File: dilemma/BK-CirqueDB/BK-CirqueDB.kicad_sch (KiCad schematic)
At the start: 9 parts, among them J1 CirqueDB

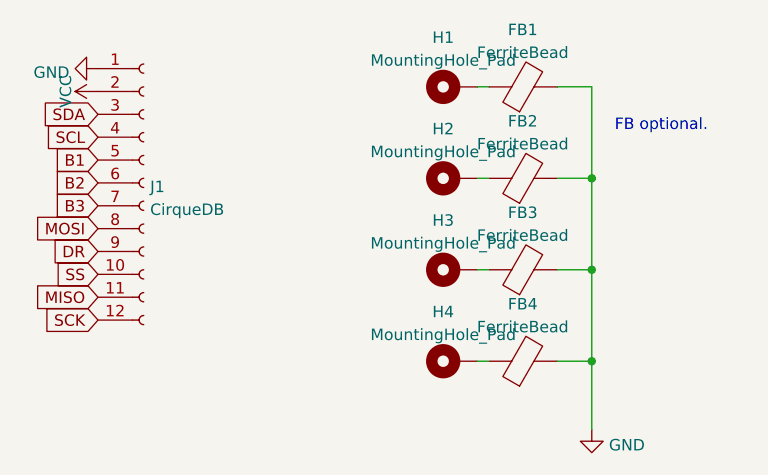
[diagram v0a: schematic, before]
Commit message: make trackpad pinout compatible with oled
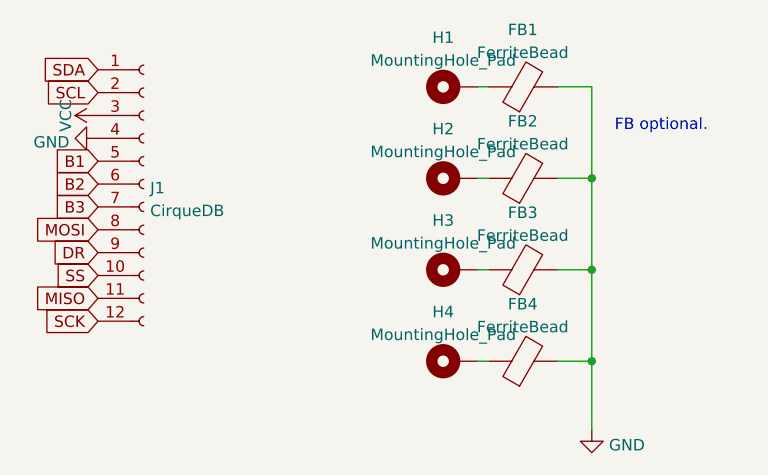
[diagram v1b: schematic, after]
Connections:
- net GND: now also J1.4 (Pin_4); no longer J1.1 (Pin_1)
- net SCL: now also J1.2 (Pin_2); no longer J1.4 (Pin_4)
- net SDA: now also J1.1 (Pin_1); no longer J1.3 (Pin_3)
- net VCC: now also J1.3 (Pin_3); no longer J1.2 (Pin_2)
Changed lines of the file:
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@@
     (effects (font (size 1.27 1.27)) (justify left bottom))
   )
-  (global_label "B1" (shape input) (at 27.94 33.528 180) (fields_autoplaced)
-    (effects (font (size 1.27 1.27)) (justify right))
-    (property "Intersheet References" "${INTERSHEET_REFS}" (id 0) (at 23.0474 33.4486 0)
-      (effects (font (size 1.27 1.27)) (justify right) hide)
-    )
-  )
-  (global_label "MOSI" (shape input) (at 27.94 41.148 180) (fields_autoplaced)
-    (effects (font (size 1.27 1.27)) (justify right))
-    (property "Intersheet References" "${INTERSHEET_REFS}" (id 0) (at 20.9307 41.0686 0)
-      (effects (font (size 1.27 1.27)) (justify right) hide)
-    )
-  )
-  (global_label "DR" (shape input) (at 27.94 43.688 180) (fields_autoplaced)
-    (effects (font (size 1.27 1.27)) (justify right))
-    (property "Intersheet References" "${INTERSHEET_REFS}" (id 0) (at 22.9869 43.6086 0)
-      (effects (font (size 1.27 1.27)) (justify right) hide)
-    )
-  )
-  (global_label "B3" (shape input) (at 27.94 38.608 180) (fields_autoplaced)
-    (effects (font (size 1.27 1.27)) (justify right))
-    (property "Intersheet References" "${INTERSHEET_REFS}" (id 0) (at 23.0474 38.5286 0)
-      (effects (font (size 1.27 1.27)) (justify right) hide)
-    )
-  )
-  (global_label "MISO" (shape input) (at 27.94 48.768 180) (fields_autoplaced)
-    (effects (font (size 1.27 1.27)) (justify right))
-    (property "Intersheet References" "${INTERSHEET_REFS}" (id 0) (at 20.9307 48.6886 0)
-      (effects (font (size 1.27 1.27)) (justify right) hide)
-    )
-  )
-  (global_label "B2" (shape input) (at 27.94 36.068 180) (fields_autoplaced)
-    (effects (font (size 1.27 1.27)) (justify right))
-    (property "Intersheet References" "${INTERSHEET_REFS}" (id 0) (at 23.0474 35.9886 0)
-      (effects (font (size 1.27 1.27)) (justify right) hide)
-    )
-  )
-  (global_label "SDA" (shape input) (at 27.94 28.448 180) (fields_autoplaced)
-    (effects (font (size 1.27 1.27)) (justify right))
-    (property "Intersheet References" "${INTERSHEET_REFS}" (id 0) (at 21.9588 28.3686 0)
-      (effects (font (size 1.27 1.27)) (justify right) hide)
-    )
-  )
-  (global_label "SCL" (shape input) (at 27.94 30.988 180) (fields_autoplaced)
-    (effects (font (size 1.27 1.27)) (justify right))
-    (property "Intersheet References" "${INTERSHEET_REFS}" (id 0) (at 22.0193 30.9086 0)
-      (effects (font (size 1.27 1.27)) (justify right) hide)
-    )
-  )
-  (global_label "SS" (shape input) (at 27.94 46.228 180) (fields_autoplaced)
-    (effects (font (size 1.27 1.27)) (justify right))
-    (property "Intersheet References" "${INTERSHEET_REFS}" (id 0) (at 23.1079 46.1486 0)
-      (effects (font (size 1.27 1.27)) (justify right) hide)
-    )
-  )
-  (global_label "SCK" (shape input) (at 27.94 51.308 180) (fields_autoplaced)
-    (effects (font (size 1.27 1.27)) (justify right))
-    (property "Intersheet References" "${INTERSHEET_REFS}" (id 0) (at 21.7774 51.2286 0)
-      (effects (font (size 1.27 1.27)) (justify right) hide)
-    )
-  )
-  (symbol (lib_id "Connector:Conn_01x12_Female") (at 33.02 36.068 0) (unit 1)
-    (in_bom yes) (on_board yes) (fields_autoplaced)
-    (property "Reference" "J1" (id 0) (at 33.7312 36.5033 0)
+  (global_label "B1" (shape input) (at 27.94 33.655 180) (fields_autoplaced)
+    (effects (font (size 1.27 1.27)) (justify right))
+    (property "Intersheet References" "${INTERSHEET_REFS}" (id 0) (at 23.0474 33.5756 0)
+      (effects (font (size 1.27 1.27)) (justify right) hide)
+    )
+  )
+  (global_label "MOSI" (shape input) (at 27.94 41.275 180) (fields_autoplaced)
+    (effects (font (size 1.27 1.27)) (justify right))
+    (property "Intersheet References" "${INTERSHEET_REFS}" (id 0) (at 20.9307 41.1956 0)
+      (effects (font (size 1.27 1.27)) (justify right) hide)
+    )
+  )
+  (global_label "DR" (shape input) (at 27.94 43.815 180) (fields_autoplaced)
+    (effects (font (size 1.27 1.27)) (justify right))
+    (property "Intersheet References" "${INTERSHEET_REFS}" (id 0) (at 22.9869 43.7356 0)
+      (effects (font (size 1.27 1.27)) (justify right) hide)
+    )
+  )
+  (global_label "B3" (shape input) (at 27.94 38.735 180) (fields_autoplaced)
+    (effects (font (size 1.27 1.27)) (justify right))
+    (property "Intersheet References" "${INTERSHEET_REFS}" (id 0) (at 23.0474 38.6556 0)
+      (effects (font (size 1.27 1.27)) (justify right) hide)
+    )
+  )
+  (global_label "MISO" (shape input) (at 27.94 48.895 180) (fields_autoplaced)
+    (effects (font (size 1.27 1.27)) (justify right))
+    (property "Intersheet References" "${INTERSHEET_REFS}" (id 0) (at 20.9307 48.8156 0)
+      (effects (font (size 1.27 1.27)) (justify right) hide)
+    )
+  )
+  (global_label "B2" (shape input) (at 27.94 36.195 180) (fields_autoplaced)
+    (effects (font (size 1.27 1.27)) (justify right))
+    (property "Intersheet References" "${INTERSHEET_REFS}" (id 0) (at 23.0474 36.1156 0)
+      (effects (font (size 1.27 1.27)) (justify right) hide)
+    )
+  )
+  (global_label "SDA" (shape input) (at 27.94 23.495 180) (fields_autoplaced)
+    (effects (font (size 1.27 1.27)) (justify right))
+    (property "Intersheet References" "${INTERSHEET_REFS}" (id 0) (at 21.9588 23.4156 0)
+      (effects (font (size 1.27 1.27)) (justify right) hide)
+    )
+  )
+  (global_label "SCL" (shape input) (at 27.94 26.035 180) (fields_autoplaced)
+    (effects (font (size 1.27 1.27)) (justify right))
+    (property "Intersheet References" "${INTERSHEET_REFS}" (id 0) (at 22.0193 25.9556 0)
+      (effects (font (size 1.27 1.27)) (justify right) hide)
+    )
+  )
+  (global_label "SS" (shape input) (at 27.94 46.355 180) (fields_autoplaced)
+    (effects (font (size 1.27 1.27)) (justify right))
+    (property "Intersheet References" "${INTERSHEET_REFS}" (id 0) (at 23.1079 46.2756 0)
+      (effects (font (size 1.27 1.27)) (justify right) hide)
+    )
+  )
+  (global_label "SCK" (shape input) (at 27.94 51.435 180) (fields_autoplaced)
+    (effects (font (size 1.27 1.27)) (justify right))
+    (property "Intersheet References" "${INTERSHEET_REFS}" (id 0) (at 21.7774 51.3556 0)
+      (effects (font (size 1.27 1.27)) (justify right) hide)
+    )
+  )
+  (symbol (lib_id "Connector:Conn_01x12_Female") (at 33.02 36.195 0) (unit 1)
+    (in_bom yes) (on_board yes) (fields_autoplaced)
+    (property "Reference" "J1" (id 0) (at 33.7312 36.6303 0)
       (effects (font (size 1.27 1.27)) (justify left))
     )
-    (property "Value" "CirqueDB" (id 1) (at 33.7312 39.0402 0)
+    (property "Value" "CirqueDB" (id 1) (at 33.7312 39.1672 0)
       (effects (font (size 1.27 1.27)) (justify left))
     )
-    (property "Footprint" "prettylib:CirqueDB-BK" (id 2) (at 33.02 36.068 0)
-      (effects (font (size 1.27 1.27)) hide)
-    )
-    (property "Datasheet" "~" (id 3) (at 33.02 36.068 0)
+    (property "Footprint" "prettylib:CirqueDB-BK" (id 2) (at 33.02 36.195 0)
+      (effects (font (size 1.27 1.27)) hide)
+    )
+    (property "Datasheet" "~" (id 3) (at 33.02 36.195 0)
       (effects (font (size 1.27 1.27)) hide)
     )
@@
     (pin "1")
   )
-  (symbol (lib_id "power:GND") (at 27.94 23.368 270) (unit 1)
-    (in_bom yes) (on_board yes) (fields_autoplaced)
-    (property "Reference" "#PWR0104" (id 0) (at 21.59 23.368 0)
-      (effects (font (size 1.27 1.27)) hide)
-    )
-    (property "Value" "GND" (id 1) (at 24.7651 23.8018 90)
+  (symbol (lib_id "power:GND") (at 27.94 31.115 270) (unit 1)
+    (in_bom yes) (on_board yes) (fields_autoplaced)
+    (property "Reference" "#PWR0104" (id 0) (at 21.59 31.115 0)
+      (effects (font (size 1.27 1.27)) hide)
+    )
+    (property "Value" "GND" (id 1) (at 24.7651 31.5488 90)
       (effects (font (size 1.27 1.27)) (justify right))
     )
-    (property "Footprint" "" (id 2) (at 27.94 23.368 0)
-      (effects (font (size 1.27 1.27)) hide)
-    )
-    (property "Datasheet" "" (id 3) (at 27.94 23.368 0)
+    (property "Footprint" "" (id 2) (at 27.94 31.115 0)
+      (effects (font (size 1.27 1.27)) hide)
+    )
+    (property "Datasheet" "" (id 3) (at 27.94 31.115 0)
       (effects (font (size 1.27 1.27)) hide)
     )
@@
     (pin "1")
   )
-  (symbol (lib_id "power:VCC") (at 27.94 25.908 90) (unit 1)
+  (symbol (lib_id "power:VCC") (at 27.94 28.575 90) (unit 1)
     (in_bom yes) (on_board yes)
-    (property "Reference" "#PWR0103" (id 0) (at 31.75 25.908 0)
-      (effects (font (size 1.27 1.27)) hide)
-    )
-    (property "Value" "VCC" (id 1) (at 24.3642 25.908 0))
-    (property "Footprint" "" (id 2) (at 27.94 25.908 0)
-      (effects (font (size 1.27 1.27)) hide)
-    )
-    (property "Datasheet" "" (id 3) (at 27.94 25.908 0)
-      (effects (font (size 1.27 1.27)) hide)
-    )
+    (property "Reference" "#PWR0103" (id 0) (at 31.75 28.575 0)
+      (effects (font (size 1.27 1.27)) hide)
+    )
+    (property "Value" "VCC" (id 1) (at 24.3642 28.575 0))
+    (property "Footprint" "" (id 2) (at 27.94 28.575 0)
+      (effects (font (size 1.27 1.27)) hide)
+    )
+    (property "Datasheet" "" (id 3) (at 27.94 28.575 0)
+      (effects (font (size 1.27 1.27)) hide)
+    )
